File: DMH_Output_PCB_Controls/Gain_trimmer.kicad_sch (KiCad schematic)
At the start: 10 parts, among them J11 Conn_01x06_PinHeader, J26 Conn_01x06_PinHeader, U8 TL074

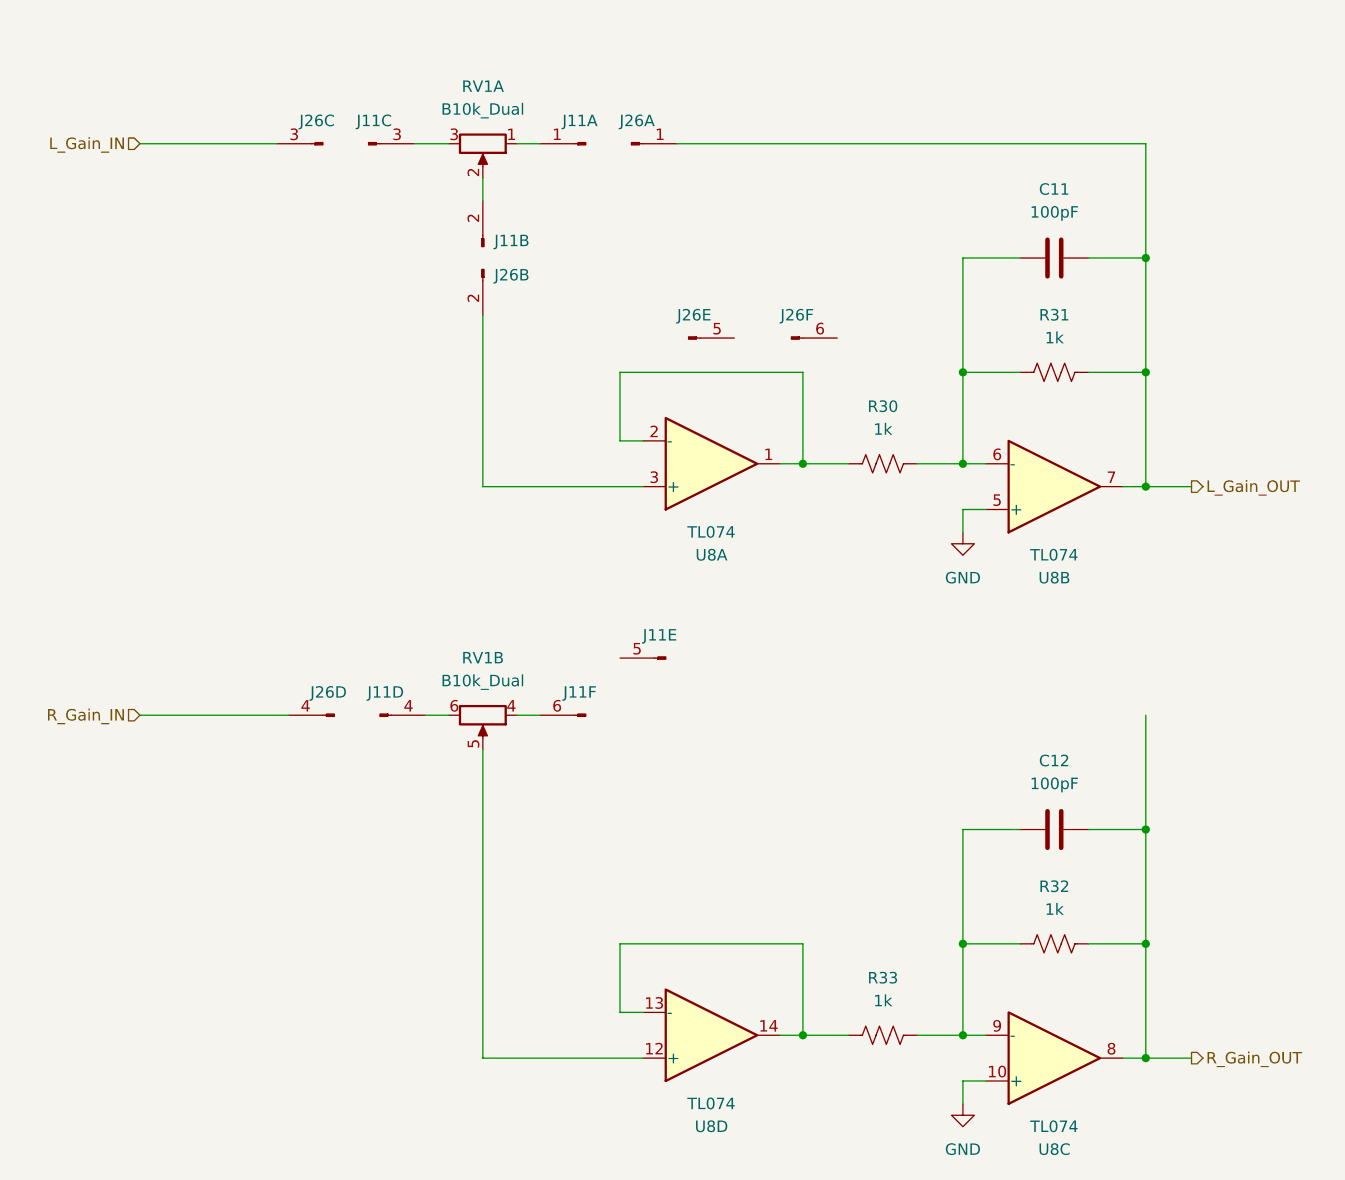
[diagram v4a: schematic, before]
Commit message: Clarified interPCB connectors in schematic
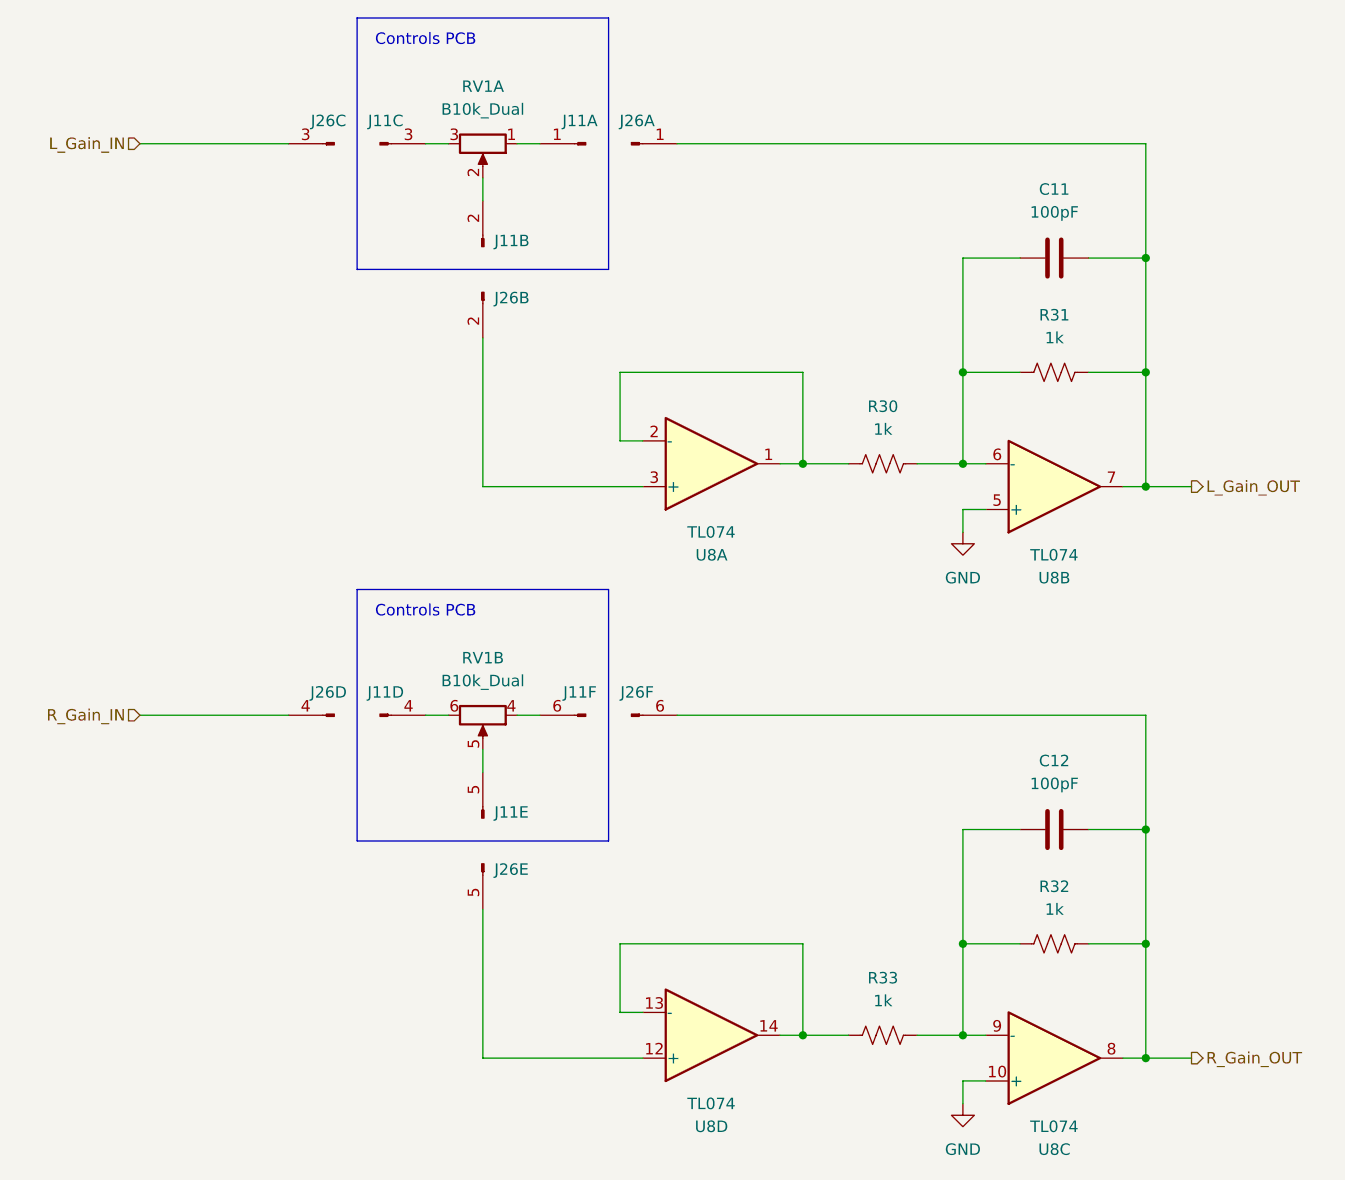
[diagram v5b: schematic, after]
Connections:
- net R_Gain_OUT: now also J26.6 (Pin_6)
- net at U8.12 (+): now also J26.5 (Pin_5); no longer RV1.5
- net at J11.5 (Pin_5): now also RV1.5
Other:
- note added: "Controls PCB"
- moved on the sheet: J11C, J11E, J26B, J26C, J26E, J26F
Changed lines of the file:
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@@
 		(comment 1 "PCB for 5 cm Kosmo format synthesizer module")
+	)
+	(rectangle
+		(start 62.23 100.33)
+		(end 90.17 128.27)
+		(stroke
+			(width 0)
+			(type default)
+		)
+		(fill
+			(type none)
+		)
+	)
+	(rectangle
+		(start 62.23 36.83)
+		(end 90.17 64.77)
+		(stroke
+			(width 0)
+			(type default)
+		)
+		(fill
+			(type none)
+		)
+	)
+	(text "Controls PCB"
+		(exclude_from_sim no)
+		(at 69.85 102.87 0)
+		(effects
+			(font
+				(size 1.27 1.27)
+			)
+		)
+	)
+	(text "Controls PCB"
+		(exclude_from_sim no)
+		(at 69.85 39.37 0)
+		(effects
+			(font
+				(size 1.27 1.27)
+			)
+		)
 	)
 	(junction
@@
 	(wire
 		(pts
-			(xy 76.2 69.85) (xy 76.2 88.9)
+			(xy 76.2 72.39) (xy 76.2 88.9)
 		)
 		(stroke
@@
 	(wire
 		(pts
-			(xy 68.58 50.8) (xy 72.39 50.8)
+			(xy 69.85 50.8) (xy 72.39 50.8)
 		)
 		(stroke
@@
 	(wire
 		(pts
-			(xy 76.2 118.11) (xy 76.2 152.4)
+			(xy 76.2 118.11) (xy 76.2 120.65)
 		)
 		(stroke
@@
 	(wire
 		(pts
+			(xy 76.2 135.89) (xy 76.2 152.4)
+		)
+		(stroke
+			(width 0)
+			(type default)
+		)
+	)
+	(wire
+		(pts
 			(xy 111.76 139.7) (xy 111.76 149.86)
 		)
@@
 	(wire
 		(pts
-			(xy 38.1 50.8) (xy 53.34 50.8)
+			(xy 38.1 50.8) (xy 54.61 50.8)
 		)
 		(stroke
@@
 		(pts
 			(xy 143.51 139.7) (xy 149.86 139.7)
+		)
+		(stroke
+			(width 0)
+			(type default)
+		)
+	)
+	(wire
+		(pts
+			(xy 97.79 114.3) (xy 149.86 114.3)
 		)
 		(stroke
@@
 	(symbol
 		(lib_id "SynthStuff:Conn_01x06_PinHeader")
-		(at 76.2 64.77 270)
+		(at 76.2 67.31 270)
 		(unit 2)
 		(exclude_from_sim no)
 		(in_bom yes)
-		(on_board yes)
+		(on_board no)
 		(dnp no)
 		(fields_autoplaced yes)
 		(property "Reference" "J26"
-			(at 77.47 65.4049 90)
+			(at 77.47 67.9449 90)
 			(effects
 				(font
@@
 		)
 		(property "Value" "Conn_01x06_PinHeader"
-			(at 73.66 64.77 0)
+			(at 73.66 67.31 0)
 			(effects
 				(font
@@
 		)
 		(property "Footprint" "Connector_PinHeader_2.54mm:PinHeader_1x06_P2.54mm_Vertical"
-			(at 76.2 64.77 0)
+			(at 76.2 67.31 0)
 			(effects
 				(font
@@
 		)
 		(property "Datasheet" "~"
-			(at 76.2 64.77 0)
+			(at 76.2 67.31 0)
 			(effects
 				(font
@@
 		)
 		(property "Description" "Generic connector, single row, 01x06"
-			(at 76.2 64.77 0)
+			(at 76.2 67.31 0)
 			(effects
 				(font
@@
 	(symbol
 		(lib_id "SynthStuff:Conn_01x06_PinHeader")
-		(at 58.42 50.8 180)
+		(at 59.69 50.8 180)
 		(unit 3)
 		(exclude_from_sim no)
 		(in_bom yes)
-		(on_board yes)
+		(on_board no)
 		(dnp no)
 		(fields_autoplaced yes)
 		(property "Reference" "J26"
-			(at 57.785 48.26 0)
+			(at 59.055 48.26 0)
 			(effects
 				(font
@@
 		)
 		(property "Value" "Conn_01x06_PinHeader"
-			(at 58.42 48.26 0)
+			(at 59.69 48.26 0)
 			(effects
 				(font
@@
 		)
 		(property "Footprint" "Connector_PinHeader_2.54mm:PinHeader_1x06_P2.54mm_Vertical"
-			(at 58.42 50.8 0)
+			(at 59.69 50.8 0)
 			(effects
 				(font
@@
 		)
 		(property "Datasheet" "~"
-			(at 58.42 50.8 0)
+			(at 59.69 50.8 0)
 			(effects
 				(font
@@
 		)
 		(property "Description" "Generic connector, single row, 01x06"
-			(at 58.42 50.8 0)
+			(at 59.69 50.8 0)
 			(effects
 				(font
@@
 	(symbol
 		(lib_id "SynthStuff:Conn_01x06_PinHeader")
-		(at 63.5 50.8 0)
+		(at 64.77 50.8 0)
 		(unit 3)
 		(exclude_from_sim no)
@@
 		(fields_autoplaced yes)
 		(property "Reference" "J11"
-			(at 64.135 48.26 0)
+			(at 65.405 48.26 0)
 			(effects
 				(font
@@
 		)
 		(property "Value" "Conn_01x06_PinHeader"
-			(at 63.5 53.34 0)
+			(at 64.77 53.34 0)
 			(effects
 				(font
@@
 		)
 		(property "Footprint" "Connector_PinSocket_2.54mm:PinSocket_1x06_P2.54mm_Vertical"
-			(at 63.5 50.8 0)
+			(at 64.77 50.8 0)
 			(effects
 				(font
@@
 		)
 		(property "Datasheet" "~"
-			(at 63.5 50.8 0)
+			(at 64.77 50.8 0)
 			(effects
 				(font
@@
 		)
 		(property "Description" "Generic connector, single row, 01x06"
-			(at 63.5 50.8 0)
+			(at 64.77 50.8 0)
 			(effects
 				(font
@@
 		(exclude_from_sim no)
 		(in_bom yes)
-		(on_board yes)
+		(on_board no)
 		(dnp no)
 		(fields_autoplaced yes)
@@
 	(symbol
 		(lib_id "SynthStuff:Conn_01x06_PinHeader")
-		(at 110.49 72.39 0)
+		(at 92.71 114.3 0)
 		(unit 6)
 		(exclude_from_sim no)
 		(in_bom yes)
-		(on_board yes)
+		(on_board no)
 		(dnp no)
 		(fields_autoplaced yes)
 		(property "Reference" "J26"
-			(at 111.125 69.85 0)
+			(at 93.345 111.76 0)
 			(effects
 				(font
@@
 		)
 		(property "Value" "Conn_01x06_PinHeader"
-			(at 110.49 74.93 0)
+			(at 92.71 116.84 0)
 			(effects
 				(font
@@
 		)
 		(property "Footprint" "Connector_PinHeader_2.54mm:PinHeader_1x06_P2.54mm_Vertical"
-			(at 110.49 72.39 0)
+			(at 92.71 114.3 0)
 			(effects
 				(font
@@
 		)
 		(property "Datasheet" "~"
-			(at 110.49 72.39 0)
+			(at 92.71 114.3 0)
 			(effects
 				(font
@@
 		)
 		(property "Description" "Generic connector, single row, 01x06"
-			(at 110.49 72.39 0)
+			(at 92.71 114.3 0)
 			(effects
 				(font
@@
 		(exclude_from_sim no)
 		(in_bom yes)
-		(on_board yes)
+		(on_board no)
 		(dnp no)
 		(fields_autoplaced yes)
@@
 	(symbol
 		(lib_id "SynthStuff:Conn_01x06_PinHeader")
-		(at 99.06 72.39 0)
+		(at 76.2 130.81 270)
 		(unit 5)
 		(exclude_from_sim no)
 		(in_bom yes)
-		(on_board yes)
+		(on_board no)
 		(dnp no)
 		(fields_autoplaced yes)
 		(property "Reference" "J26"
-			(at 99.695 69.85 0)
-			(effects
-				(font
-					(size 1.27 1.27)
-				)
+			(at 77.47 131.4449 90)
+			(effects
+				(font
+					(size 1.27 1.27)
+				)
+				(justify left)
 			)
 		)
 		(property "Value" "Conn_01x06_PinHeader"
-			(at 99.06 74.93 0)
+			(at 73.66 130.81 0)
 			(effects
 				(font
@@
 		)
 		(property "Footprint" "Connector_PinHeader_2.54mm:PinHeader_1x06_P2.54mm_Vertical"
-			(at 99.06 72.39 0)
+			(at 76.2 130.81 0)
 			(effects
 				(font
@@
 		)
 		(property "Datasheet" "~"
-			(at 99.06 72.39 0)
+			(at 76.2 130.81 0)
 			(effects
 				(font
@@
 		)
 		(property "Description" "Generic connector, single row, 01x06"
-			(at 99.06 72.39 0)
+			(at 76.2 130.81 0)
 			(effects
 				(font
@@
 	(symbol
 		(lib_id "SynthStuff:Conn_01x06_PinHeader")
-		(at 96.52 107.95 180)
+		(at 76.2 125.73 90)
 		(unit 5)
 		(exclude_from_sim no)
@@
 		(fields_autoplaced yes)
 		(property "Reference" "J11"
-			(at 95.885 105.41 0)
-			(effects
-				(font
-					(size 1.27 1.27)
-				)
+			(at 77.47 125.0949 90)
+			(effects
+				(font
+					(size 1.27 1.27)
+				)
+				(justify right)
 			)
 		)
 		(property "Value" "Conn_01x06_PinHeader"
-			(at 96.52 105.41 0)
+			(at 78.74 125.73 0)
 			(effects
 				(font
@@
 		)
 		(property "Footprint" "Connector_PinSocket_2.54mm:PinSocket_1x06_P2.54mm_Vertical"
-			(at 96.52 107.95 0)
+			(at 76.2 125.73 0)
 			(effects
 				(font
@@
 		)
 		(property "Datasheet" "~"
-			(at 96.52 107.95 0)
+			(at 76.2 125.73 0)
 			(effects
 				(font
@@
 		)
 		(property "Description" "Generic connector, single row, 01x06"
-			(at 96.52 107.95 0)
-			(effects
-				(font
+			(at 76.2 125.73 0)
+			(effects
+				(font

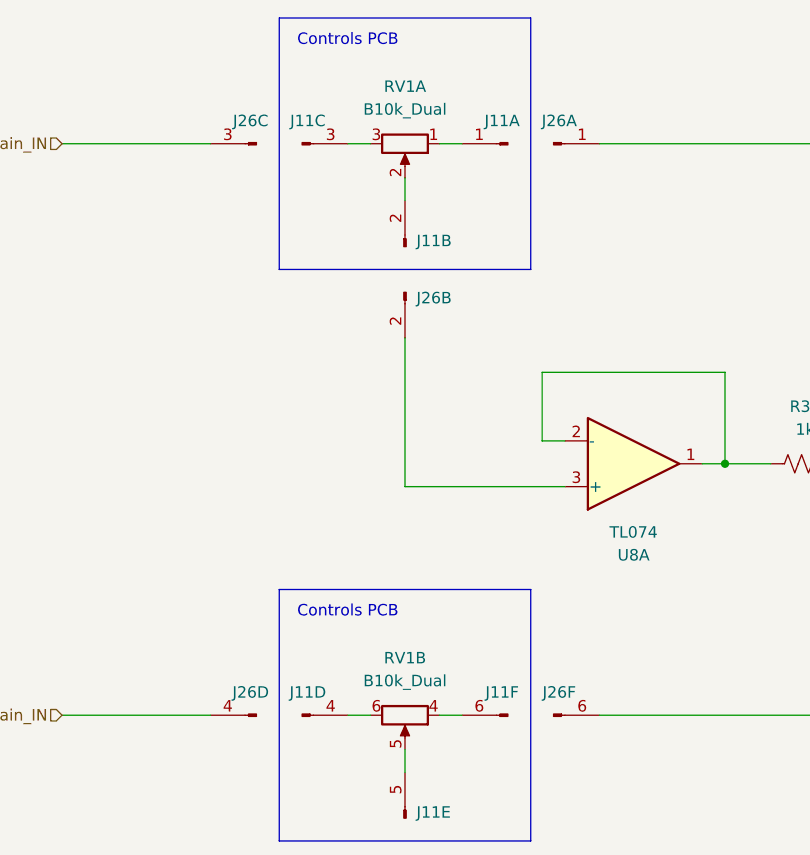
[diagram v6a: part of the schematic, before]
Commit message: Replaced jack symbols with 5pin ones
Also updated Meter LED current source resistor to 75R
Also increased LED guiding PCB mounting holes to M2.5
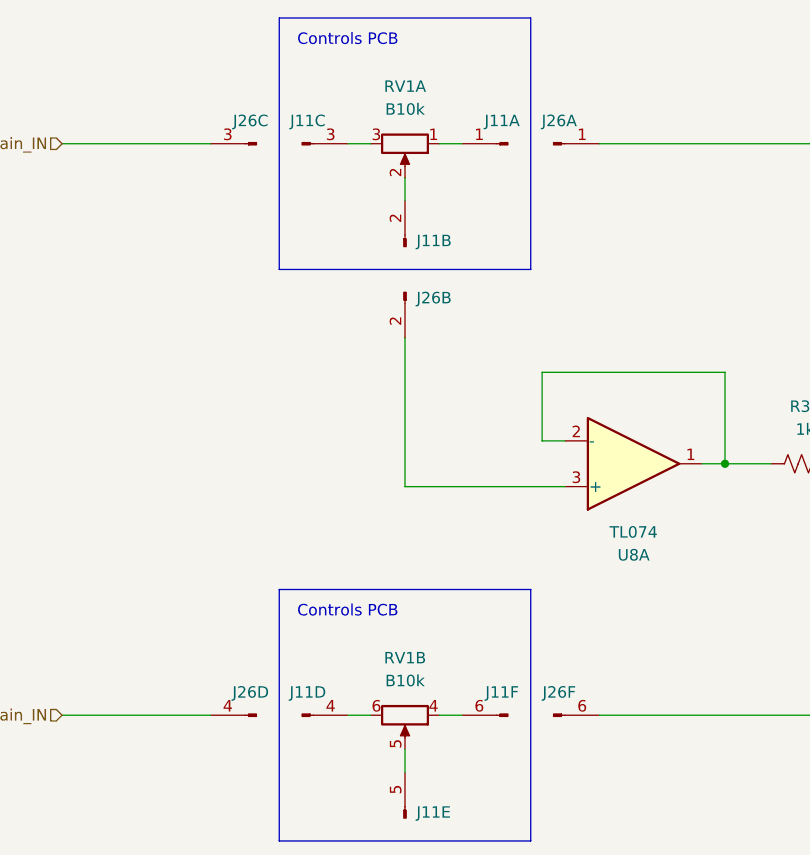
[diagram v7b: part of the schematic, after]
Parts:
- RV1: value B10k_Dual -> B10k; footprint Potentiometer_THT:Potentiometer_Alpha_RD902F-40-00D_Dual_Vertical -> SynthStuff:Potentiometer_Alpha_RD902F-40-00D_Dual_Vertical
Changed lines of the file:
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@@
 			)
 		)
-		(property "Value" "B10k_Dual"
+		(property "Value" "B10k"
 			(at 76.2 46.99 90)
 			(show_name no)
@@
 			)
 		)
-		(property "Footprint" "Potentiometer_THT:Potentiometer_Alpha_RD902F-40-00D_Dual_Vertical"
+		(property "Footprint" "SynthStuff:Potentiometer_Alpha_RD902F-40-00D_Dual_Vertical"
 			(at 76.2 50.8 0)
 			(hide yes)
@@
 					(bold yes)
 					(italic yes)
+				)
+			)
+		)
+		(property "Sim.Library" "${KICAD9_SYMBOL_DIR}/Simulation_SPICE.sp"
+			(at 76.2 50.8 0)
+			(hide yes)
+			(show_name no)
+			(do_not_autoplace no)
+			(effects
+				(font
+					(size 1.27 1.27)
+				)
+			)
+		)
+		(property "Sim.Name" "pot_dual"
+			(at 76.2 50.8 0)
+			(hide yes)
+			(show_name no)
+			(do_not_autoplace no)
+			(effects
+				(font
+					(size 1.27 1.27)
+				)
+			)
+		)
+		(property "Sim.Device" "SUBCKT"
+			(at 76.2 50.8 0)
+			(hide yes)
+			(show_name no)
+			(do_not_autoplace no)
+			(effects
+				(font
+					(size 1.27 1.27)
+				)
+			)
+		)
+		(property "Sim.Pins" "1=r1A 2=wA 3=r0A 4=r1B 5=wB 6=r0B"
+			(at 76.2 50.8 0)
+			(hide yes)
+			(show_name no)
+			(do_not_autoplace no)
+			(effects
+				(font
+					(size 1.27 1.27)
+				)
+			)
+		)
+		(property "Sim.Params" "Rtot=1 wpos=0.4"
+			(at 76.2 50.8 0)
+			(hide yes)
+			(show_name no)
+			(do_not_autoplace no)
+			(effects
+				(font
+					(size 1.27 1.27)
 				)
 			)
@@
 			)
 		)
-		(property "Value" "B10k_Dual"
+		(property "Value" "B10k"
 			(at 76.2 110.49 90)
 			(show_name no)
@@
 			)
 		)
-		(property "Footprint" "Potentiometer_THT:Potentiometer_Alpha_RD902F-40-00D_Dual_Vertical"
+		(property "Footprint" "SynthStuff:Potentiometer_Alpha_RD902F-40-00D_Dual_Vertical"
 			(at 76.2 114.3 0)
 			(hide yes)
@@
 				)
 			)
+		)
+		(property "Sim.Library" "${KICAD9_SYMBOL_DIR}/Simulation_SPICE.sp"
+			(at 76.2 114.3 0)
+			(hide yes)
+			(show_name no)
+			(do_not_autoplace no)
+			(effects
+				(font
+					(size 1.27 1.27)
+				)
+			)
+		)
+		(property "Sim.Name" "pot_dual"
+			(at 76.2 114.3 0)
+			(hide yes)
+			(show_name no)
+			(do_not_autoplace no)
+			(effects
+				(font
+					(size 1.27 1.27)
+				)
+			)
+		)
+		(property "Sim.Device" "SUBCKT"
+			(at 76.2 114.3 0)
+			(hide yes)
+			(show_name no)
+			(do_not_autoplace no)
+			(effects
+				(font
+					(size 1.27 1.27)
+				)
+			)
+		)
+		(property "Sim.Pins" "1=r1A 2=wA 3=r0A 4=r1B 5=wB 6=r0B"
+			(at 76.2 114.3 0)
+			(hide yes)
+			(show_name no)
+			(do_not_autoplace no)
+			(effects
+				(font
+					(size 1.27 1.27)
+				)
+			)
+		)
+		(property "Sim.Params" "Rtot=1 wpos=0.4"
+			(at 76.2 114.3 0)
+			(hide yes)
+			(show_name no)
+			(do_not_autoplace no)
+			(effects
+				(font
+					(size 1.27 1.27)
+				)
+			)
